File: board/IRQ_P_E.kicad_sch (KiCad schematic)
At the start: 18 parts, among them IC5 74LS219, IC6 74LS219, IC7 74LS219, IC8 74LS219, U44 74LS148, U45 74F00, U46 74LS148, U47 74F157

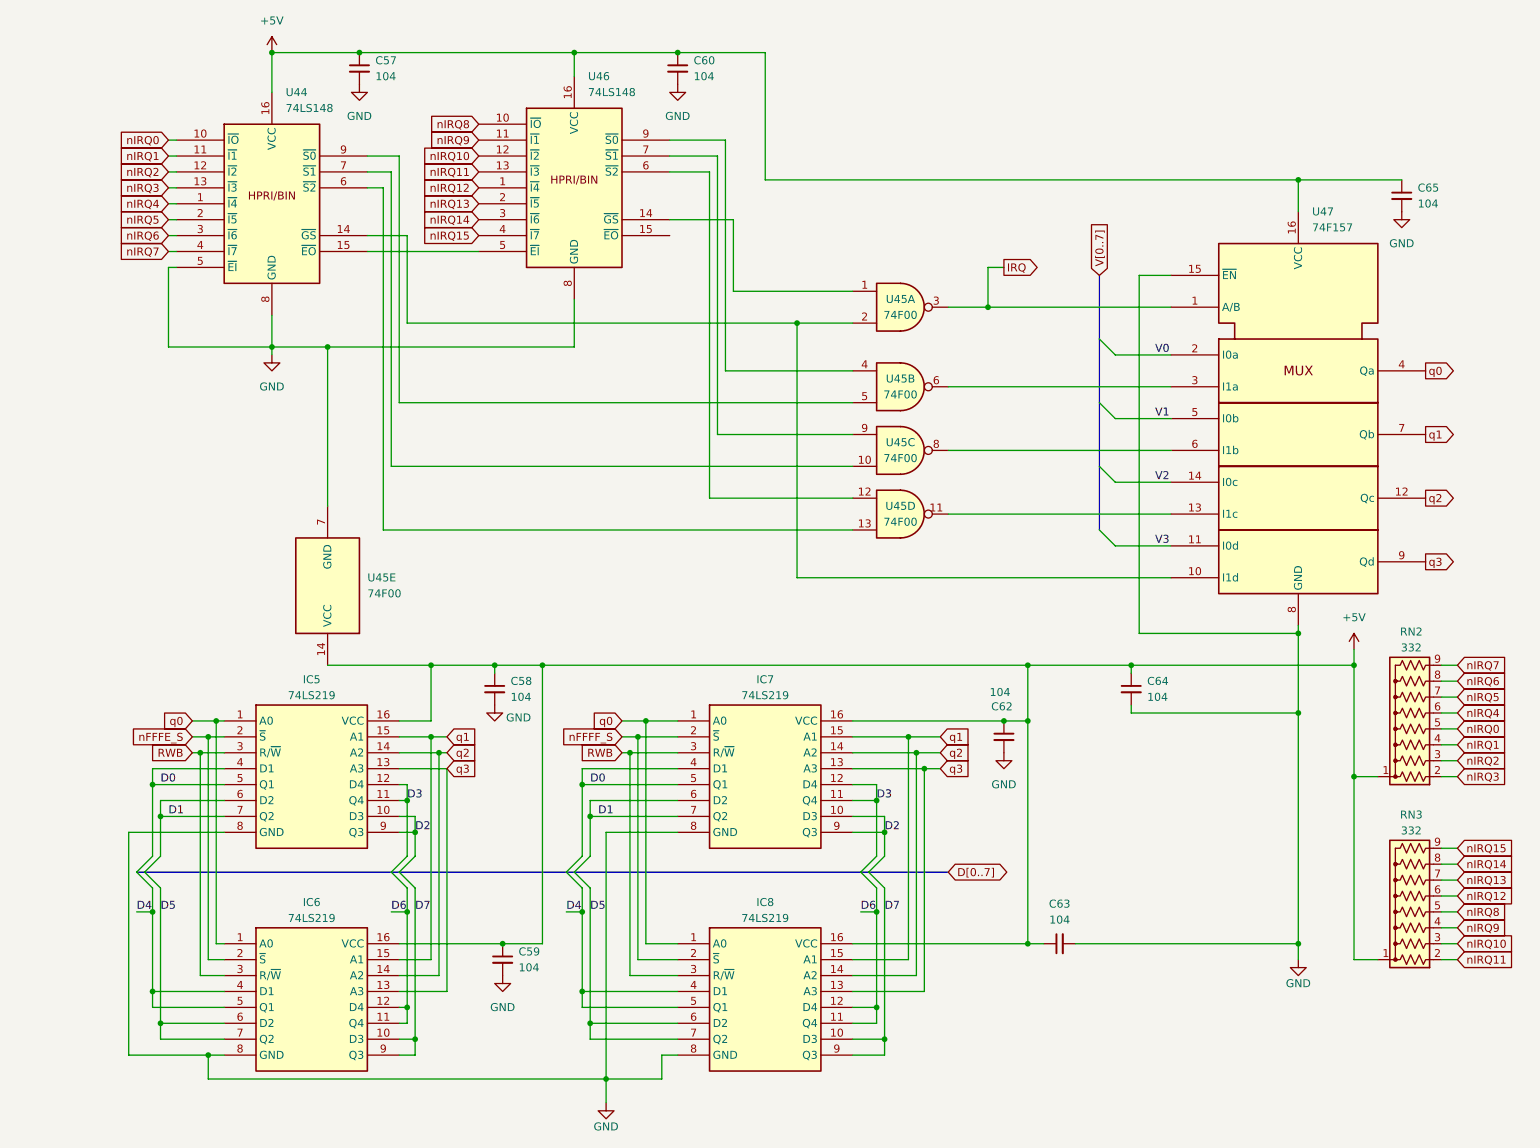
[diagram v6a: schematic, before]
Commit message: 1.7C: Logic corrections and placement tweaks
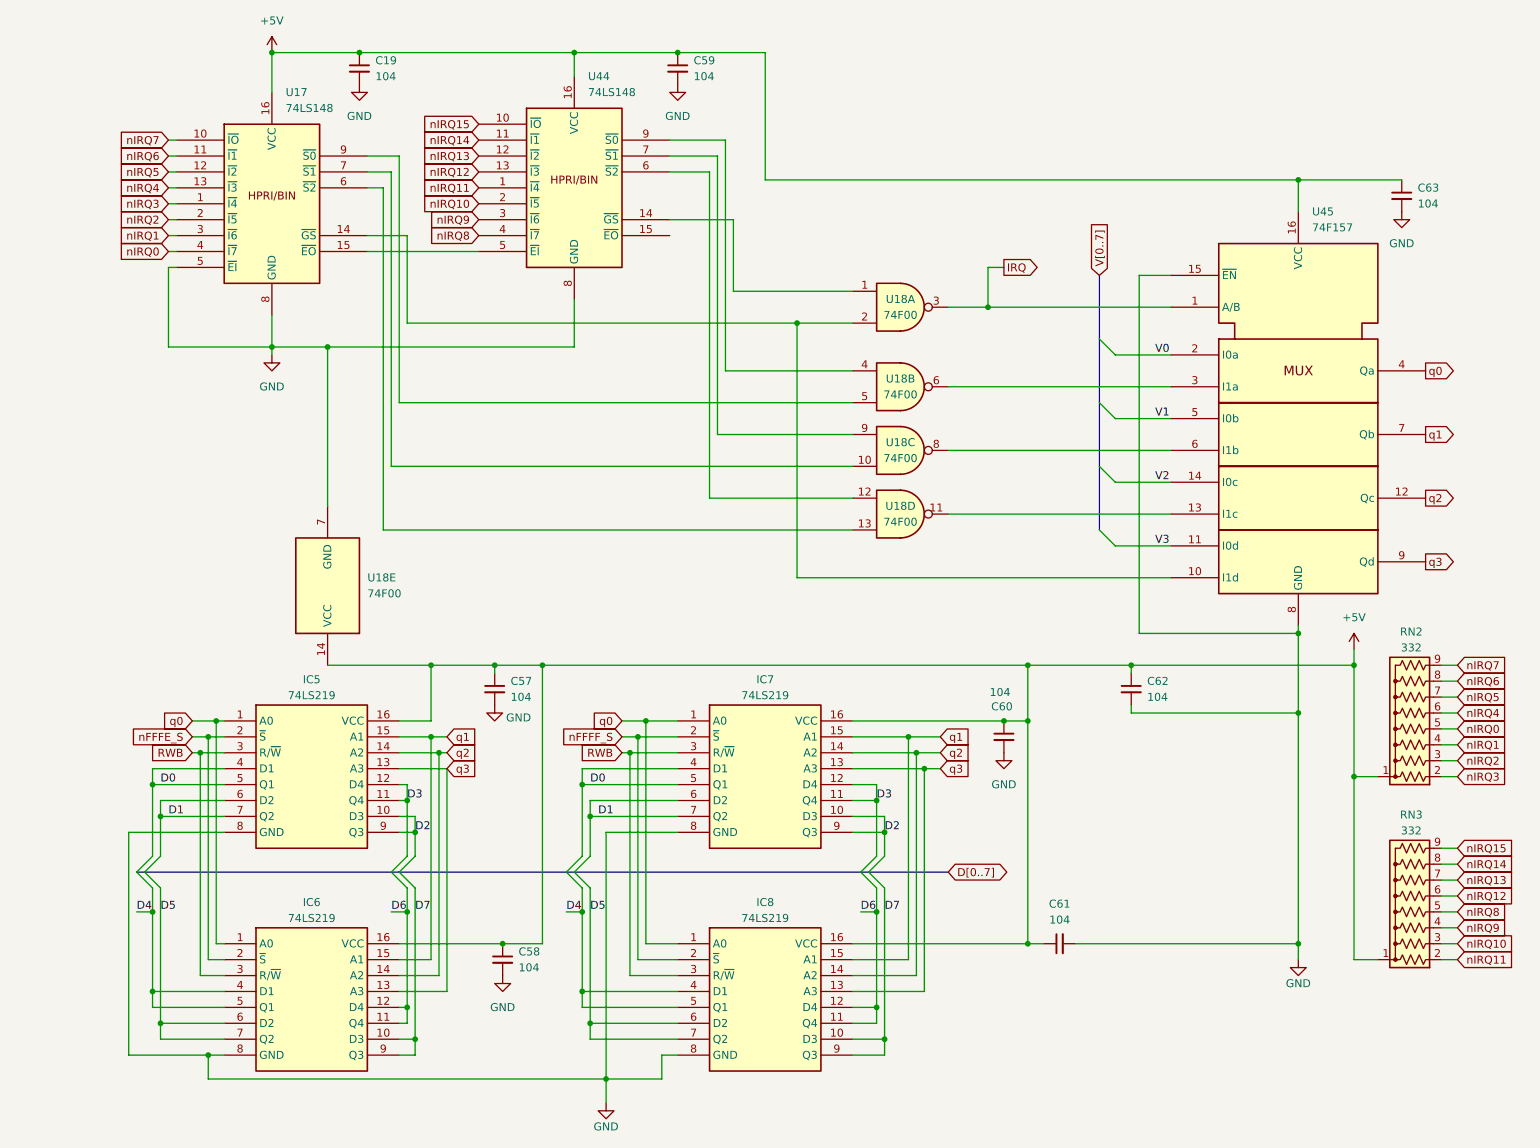
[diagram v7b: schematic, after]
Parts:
- renumbered C57 to C19, C58 to C57, C59 to C58, C60 to C59, C62 to C60, C63 to C61, C64 to C62, C65 to C63, U44 to U17, U45 to U18, U46 to U44, U47 to U45
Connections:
- net nIRQ0: now also U17.4 (~{I7}); no longer U17.10 (~{IO})
- net nIRQ1: now also U17.3 (~{I6}); no longer U17.11 (~{I1})
- net nIRQ10: now also U44.2 (~{I5}); no longer U44.12 (~{I2})
- net nIRQ11: now also U44.1 (~{I4}); no longer U44.13 (~{I3})
- net nIRQ12: now also U44.13 (~{I3}); no longer U44.1 (~{I4})
- net nIRQ13: now also U44.12 (~{I2}); no longer U44.2 (~{I5})
- net nIRQ14: now also U44.11 (~{I1}); no longer U44.3 (~{I6})
- net nIRQ15: now also U44.10 (~{IO}); no longer U44.4 (~{I7})
- net nIRQ2: now also U17.2 (~{I5}); no longer U17.12 (~{I2})
- net nIRQ3: now also U17.1 (~{I4}); no longer U17.13 (~{I3})
- net nIRQ4: now also U17.13 (~{I3}); no longer U17.1 (~{I4})
- net nIRQ5: now also U17.12 (~{I2}); no longer U17.2 (~{I5})
- net nIRQ6: now also U17.11 (~{I1}); no longer U17.3 (~{I6})
- net nIRQ7: now also U17.10 (~{IO}); no longer U17.4 (~{I7})
- net nIRQ8: now also U44.4 (~{I7}); no longer U44.10 (~{IO})
- net nIRQ9: now also U44.3 (~{I6}); no longer U44.11 (~{I1})

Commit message: V1.8C production board
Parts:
- renumbered U44 to U18, U18 to U44
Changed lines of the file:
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@@
 		(title "IRQ Priority Logic and Vector Memory")
 		(date "2025-10-01")
-		(rev "1.7C")
+		(rev "1.8A")
 		(company "Data Tuning")
 		(comment 1 "Hydra 16")
@@
 		(on_board yes)
 		(dnp no)
-		(property "Reference" "U18"
+		(property "Reference" "U44"
 			(at 154.94 72.39 0)
 			(effects
@@
 			(project "hydra-16"
 				(path "/ef29fc71-3fec-48b5-8a1a-46bee537a98c/fe0e8ec7-a78c-48fc-a3b0-2611c8b506ac"
-					(reference "U18")
+					(reference "U44")
 					(unit 2)
 				)
@@
 		(on_board yes)
 		(dnp no)
-		(property "Reference" "U18"
+		(property "Reference" "U44"
 			(at 154.94 82.55 0)
 			(effects
@@
 			(project "hydra-16"
 				(path "/ef29fc71-3fec-48b5-8a1a-46bee537a98c/fe0e8ec7-a78c-48fc-a3b0-2611c8b506ac"
-					(reference "U18")
+					(reference "U44")
 					(unit 3)
 				)
@@
 		(dnp no)
 		(fields_autoplaced yes)
-		(property "Reference" "U18"
+		(property "Reference" "U44"
 			(at 69.85 104.1399 0)
 			(effects
@@
 			(project "hydra-16"
 				(path "/ef29fc71-3fec-48b5-8a1a-46bee537a98c/fe0e8ec7-a78c-48fc-a3b0-2611c8b506ac"
-					(reference "U18")
+					(reference "U44")
 					(unit 5)
 				)
@@
 		(on_board yes)
 		(dnp no)
-		(property "Reference" "U18"
+		(property "Reference" "U44"
 			(at 154.94 59.69 0)
 			(effects
@@
 			(project "hydra-16"
 				(path "/ef29fc71-3fec-48b5-8a1a-46bee537a98c/fe0e8ec7-a78c-48fc-a3b0-2611c8b506ac"
-					(reference "U18")
+					(reference "U44")
 					(unit 1)
 				)
@@
 		(dnp no)
 		(fields_autoplaced yes)
-		(property "Reference" "U44"
-			(at 105.0641 24.13 0)
+		(property "Reference" "U18"
+			(at 105.0133 24.13 0)
 			(effects
 				(font
@@
 		)
 		(property "Value" "74LS148"
-			(at 105.0641 26.67 0)
+			(at 105.0133 26.67 0)
 			(effects
 				(font
@@
 			(project "hydra-16"
 				(path "/ef29fc71-3fec-48b5-8a1a-46bee537a98c/fe0e8ec7-a78c-48fc-a3b0-2611c8b506ac"
-					(reference "U44")
+					(reference "U18")
 					(unit 1)
 				)
@@
 		(on_board yes)
 		(dnp no)
-		(property "Reference" "U18"
+		(property "Reference" "U44"
 			(at 154.94 92.71 0)
 			(effects
@@
 			(project "hydra-16"
 				(path "/ef29fc71-3fec-48b5-8a1a-46bee537a98c/fe0e8ec7-a78c-48fc-a3b0-2611c8b506ac"
-					(reference "U18")
+					(reference "U44")
 					(unit 4)
 				)
@@
 		(fields_autoplaced yes)
 		(property "Reference" "U17"
-			(at 56.8041 26.67 0)
+			(at 56.7533 26.67 0)
 			(effects
 				(font
@@
 		)
 		(property "Value" "74LS148"
-			(at 56.8041 29.21 0)
+			(at 56.7533 29.21 0)
 			(effects
 				(font
